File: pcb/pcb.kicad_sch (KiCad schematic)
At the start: 22 parts, among them J1 Pump Back, J10 Temp & RH I2C, J2 Pump Front, J3 Electrovalve, J4 GPS, J5 Power, J6 APM, J7 Flowmeter, J8 OPC, J9 Pressure I2C, U1 LoRa, U2 MICRO SD

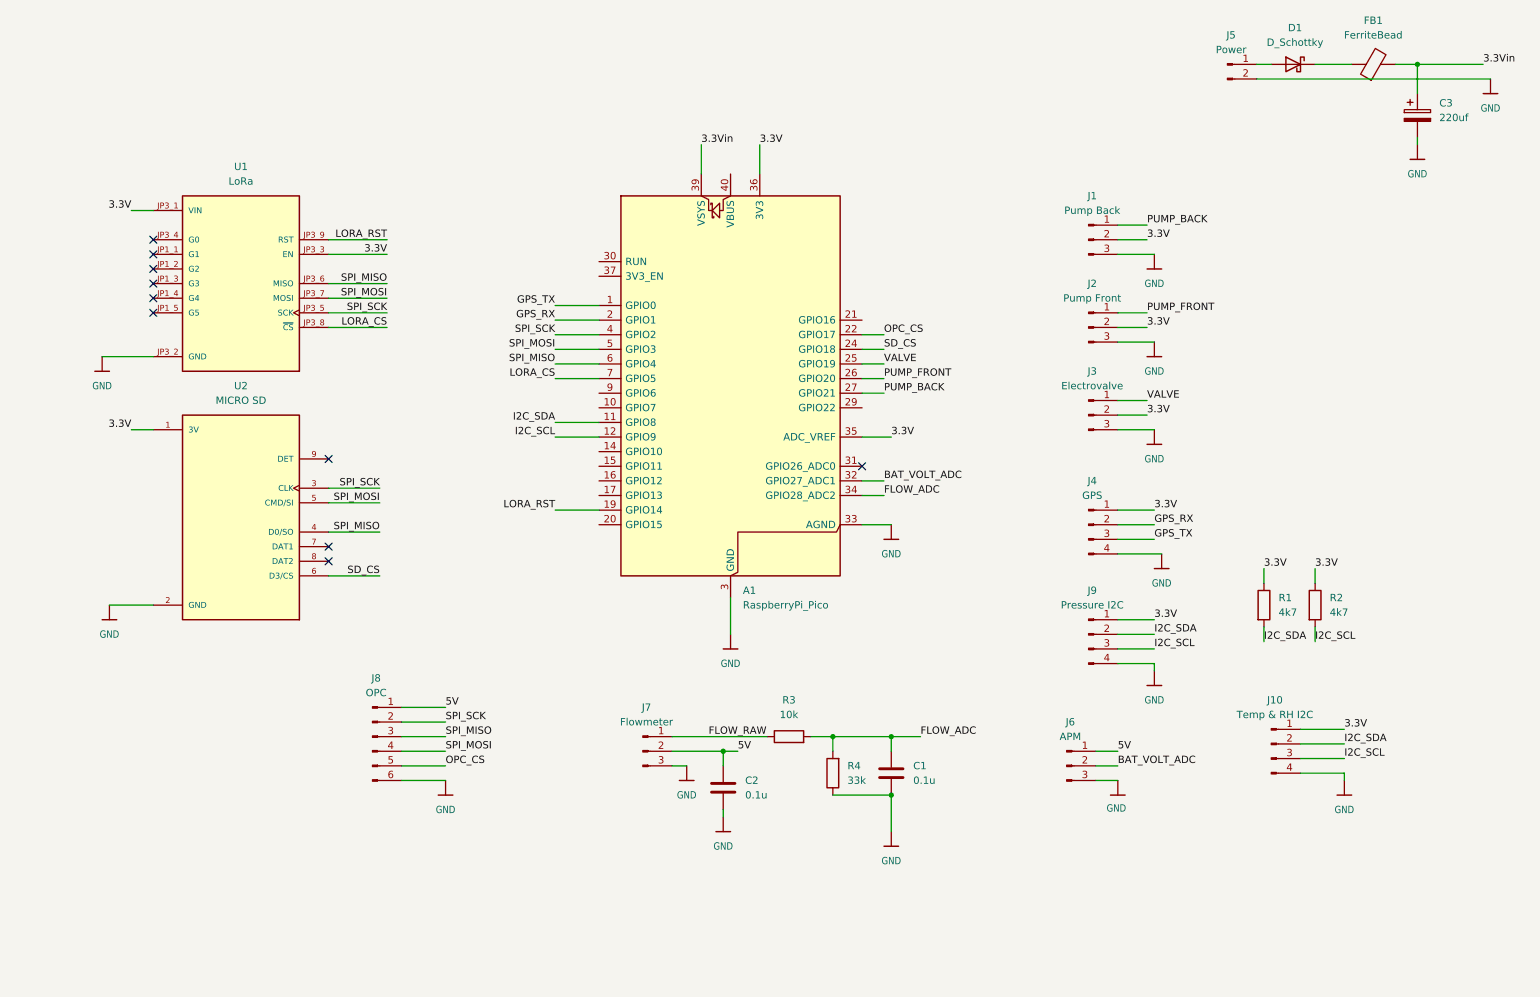
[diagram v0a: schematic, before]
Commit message: New components layout
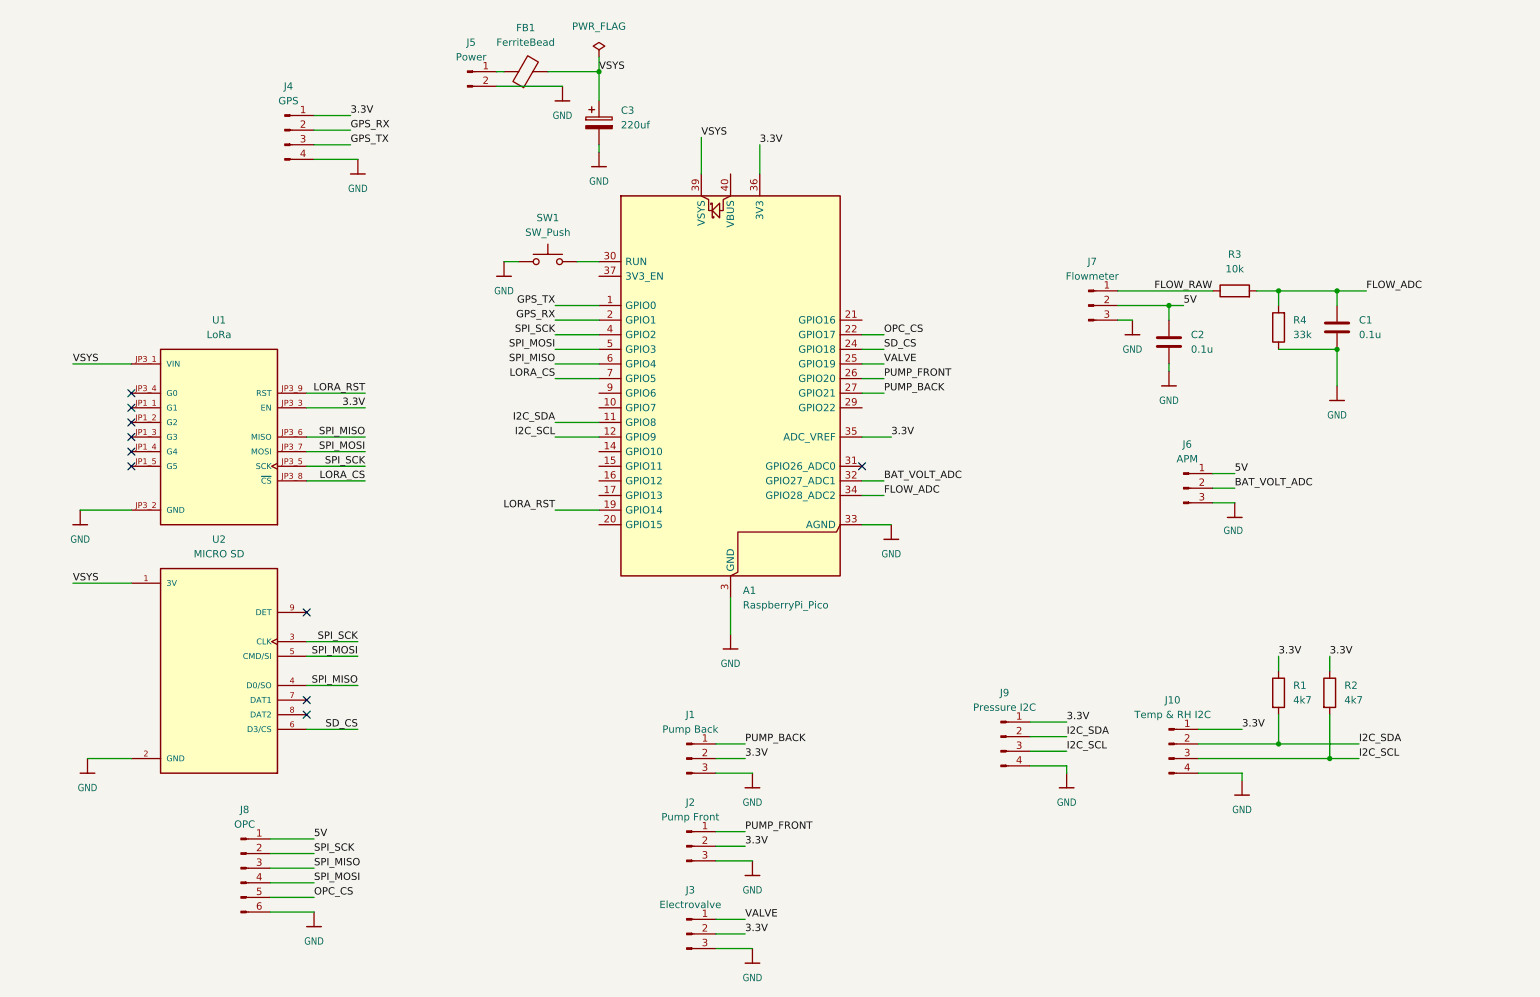
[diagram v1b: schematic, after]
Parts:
- removed D1: D_Schottky, Diode_THT:D_A-405_P7.62mm_Horizontal, symbol Device:D_Schottky
- added SW1: SW_Push, symbol Switch:SW_Push
- J1, J2, J3: footprint Connector_PinHeader_2.54mm:PinHeader_1x03_P2.54mm_Vertical -> Connector_JST:JST_XH_B3B-XH-A_1x03_P2.50mm_Vertical
- J10, J9: footprint Connector_JST:JST_EH_B4B-EH-A_1x04_P2.50mm_Vertical -> Connector_JST:JST_XH_B4B-XH-A_1x04_P2.50mm_Vertical
- J5: footprint Connector_JST:JST_EH_B2B-EH-A_1x02_P2.50mm_Vertical -> Connector_JST:JST_XH_B2B-XH-A_1x02_P2.50mm_Vertical
- J6, J7: footprint Connector_JST:JST_EH_B3B-EH-A_1x03_P2.50mm_Vertical -> Connector_JST:JST_XH_B3B-XH-A_1x03_P2.50mm_Vertical
- J8: footprint Connector_JST:JST_EH_B6B-EH-A_1x06_P2.50mm_Vertical -> Connector_JST:JST_XH_B6B-XH-A_1x06_P2.50mm_Vertical
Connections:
- net 3.3V: no longer U1.JP3_1 (VIN), U2.1 (3V)
- net GND: now also SW1.1
- net at J5.1 (Pin_1): now also FB1.1
- net at A1.30 (RUN): now also SW1.2
- net 3.3Vin renamed VSYS
- net VSYS: now also U1.JP3_1 (VIN), U2.1 (3V)
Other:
- moved on the sheet: C1, C2, C3, FB1, J1, J10, J2, J3, J4, J5, J6, J7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

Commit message: v1 sent to JLCPCB
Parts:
- SW1: footprint (none) -> Button_Switch_THT:SW_PUSH_6mm
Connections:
- net 3.3V: no longer U1.JP3_3 (EN)
- net GND: now also J2.1 (Pin_1), J3.1 (Pin_1), J4.2 (Pin_2), J8.2 (Pin_2); no longer J2.3 (Pin_3), J3.3 (Pin_3), J4.4 (Pin_4), J8.6 (Pin_6)
- net GPS_RX: now also J4.3 (Pin_3); no longer J4.2 (Pin_2)
- net GPS_TX: now also J4.4 (Pin_4); no longer J4.3 (Pin_3)
- net I2C_SCL: now also A1.5 (GPIO3), J10.2 (Pin_2), J9.2 (Pin_2), R1.2; no longer A1.12 (GPIO9), J10.3 (Pin_3), J9.3 (Pin_3), R2.2
- net I2C_SDA: now also A1.4 (GPIO2), J10.3 (Pin_3), J9.3 (Pin_3), R2.2; no longer A1.11 (GPIO8), J10.2 (Pin_2), J9.2 (Pin_2), R1.2
- net LORA_CS: now also A1.21 (GPIO16); no longer A1.7 (GPIO5)
- net OPC_CS: now also J8.3 (Pin_3); no longer J8.5 (Pin_5)
- net PUMP_FRONT: now also A1.9 (GPIO6), J2.3 (Pin_3); no longer A1.26 (GPIO20), J2.1 (Pin_1)
- net SD_CS: now also A1.12 (GPIO9); no longer A1.24 (GPIO18)
- net SPI_MISO: now also A1.16 (GPIO12), J8.5 (Pin_5); no longer A1.6 (GPIO4), J8.3 (Pin_3)
- net SPI_MOSI: now also A1.15 (GPIO11), J8.6 (Pin_6); no longer A1.5 (GPIO3), J8.4 (Pin_4)
- net SPI_SCK: now also A1.14 (GPIO10), J8.4 (Pin_4); no longer A1.4 (GPIO2), J8.2 (Pin_2)
- net VALVE: now also A1.10 (GPIO7), J3.3 (Pin_3); no longer A1.25 (GPIO19), J3.1 (Pin_1)
- net LORA_RST: no longer names the net of U1.JP3_9 (RST)
- net LORA_RST: no longer A1.19 (GPIO14)
- no-connect marks 10 -> 22
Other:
- moved on the sheet: C1, C2, C3, FB1, J1, J10, J2, J3, J4, J5, J6, J7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
